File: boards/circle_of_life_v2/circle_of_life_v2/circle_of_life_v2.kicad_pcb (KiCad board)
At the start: 2 copper layers, 70.9 x 96.4 mm, 118 parts, among them IC1 ESP32-WROOM-32E-N8R2, IC2 CP2102C-A01-GQFN28, IC3 TC1262-3.3VDB, IC4 TPS565242DRLR, IC5 LT3922EUFD#PBF, J1 UART Programmer, J2 JTAG Connector, J3 Servo Motor Connector, J4 Power Connector, J5 Water Pump Connector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

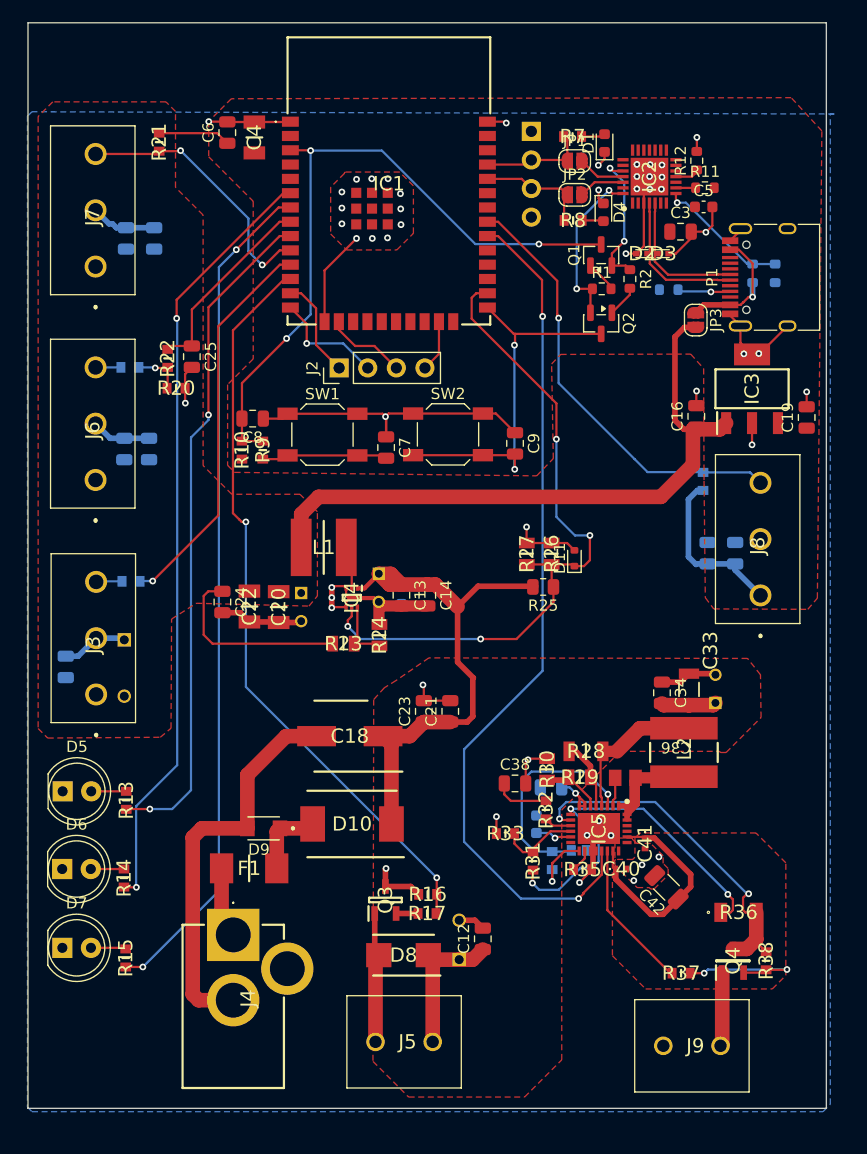
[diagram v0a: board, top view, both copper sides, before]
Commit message: Added PCB V2
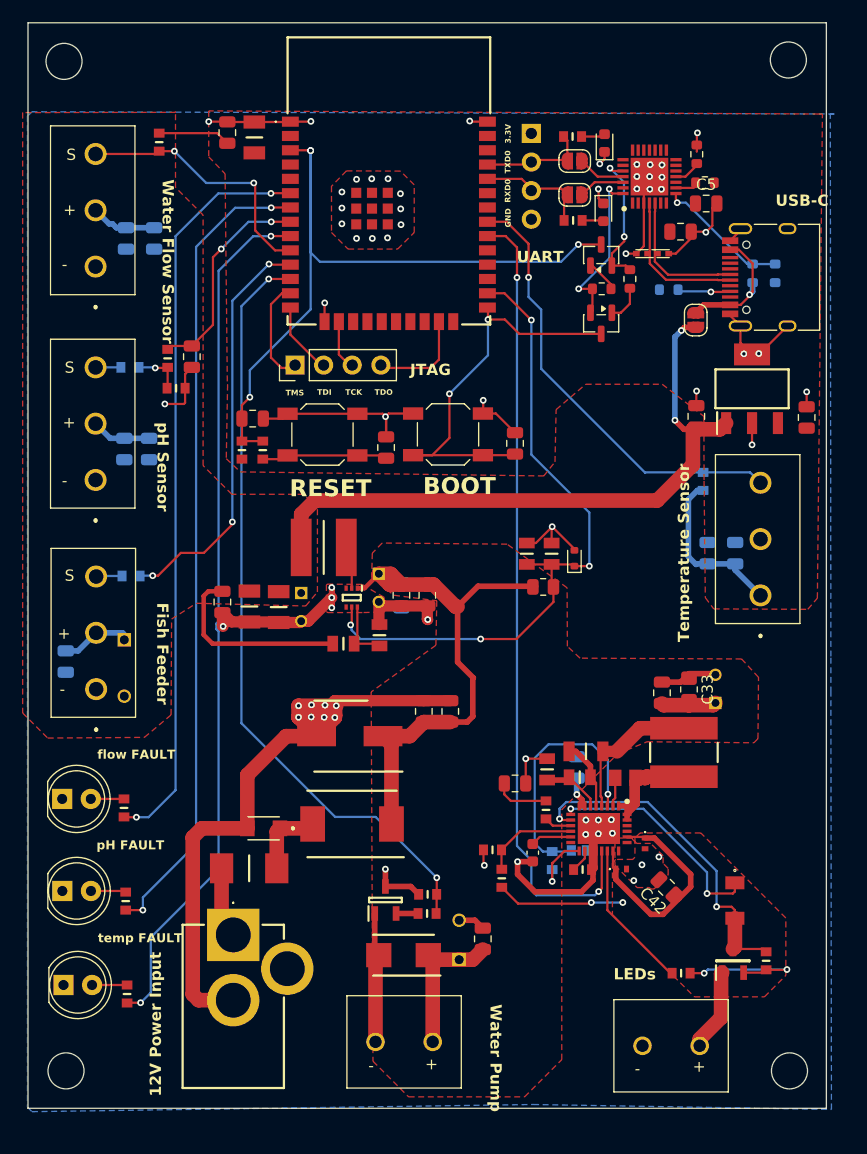
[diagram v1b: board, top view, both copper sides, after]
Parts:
- added H1: MountingHole, MountingHole:MountingHole_3.2mm_M3_ISO7380, F.Cu at (116.2, 29.3)
- added H2: MountingHole, MountingHole:MountingHole_3.2mm_M3_ISO7380, F.Cu at (180.6, 29.2)
- added H3: MountingHole, MountingHole:MountingHole_3.2mm_M3_ISO7380, F.Cu at (180.7, 119.0)
- added H4: MountingHole, MountingHole:MountingHole_3.2mm_M3_ISO7380, F.Cu at (116.4, 119.0)
- C15: footprint Capacitor_SMD:C_0603_1608Metric -> Capacitor_SMD:C_0805_2012Metric_Pad1.18x1.45mm_HandSolder
- C33: footprint SamacSys_Parts:CAPC3216X180N -> Resistor_SMD:R_0805_2012Metric_Pad1.20x1.40mm_HandSolder
- C39: moved to F.Cu
- C42: footprint Capacitor_SMD:C_1206_3216Metric -> Capacitor_SMD:C_0805_2012Metric
- C5: footprint Capacitor_SMD:C_0603_1608Metric -> Capacitor_SMD:C_0805_2012Metric
- moved R13 17.2 mm to (121.8, 112.2)
- moved D5 17.2 mm to (116.2, 111.3)
- moved D6 6.22 mm to (116.1, 94.8)
- moved R14 6.22 mm to (121.6, 95.6)
- moved D7 5.05 mm to (116.1, 103.0)
- moved R15 5.05 mm to (121.7, 103.9)
- moved J2 3.92 mm to (136.8, 56.3)
- moved R31 3.17 mm to (155.1, 101.9)
- moved C37 2.89 mm to (161.8, 92.0), turned to -90 degrees
- moved C39 2.55 mm to (157.9, 99.6), turned to 90 degrees
- moved R33 1.85 mm to (154.3, 99.3)
- moved J9 1.85 mm to (172.7, 116.8)
- moved R36 1.10 mm to (175.8, 103.8), turned to -90 degrees
- moved R12 0.57 mm to (172.4, 37.6)
- moved C1 0.47 mm to (116.4, 82.6)
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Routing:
- net GND: track 176.0 -> 204.5 mm, vias 50 -> 65
- net PH_FAULT: track 59.9 -> 76.9 mm
- net MCU_EN: track 61.5 -> 67.8 mm, vias 3 -> 4
- net PWM_DIM: track 76.6 -> 70.7 mm
- net TDO: track 4.63 -> 8.83 mm
- net TDI: track 10.1 -> 6.58 mm, vias 1 -> 0
- net INTV: track 19.9 -> 22.8 mm
- net ISP: track 54.2 -> 51.2 mm, vias 3 -> 4
- net IO0: track 33.7 -> 36.5 mm
- net TEMP_FAULT: track 75.0 -> 72.2 mm
- net TCK: track 7.23 -> 4.60 mm
- net FLOW_FAULT: track 68.9 -> 66.6 mm
- net PUMP_SGN: track 66.5 -> 68.6 mm
- net Net-(IC5-CTRL): track 4.84 -> 3.17 mm
- net SRV_SGN: track 34.8 -> 36.5 mm, vias 1 -> 3
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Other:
- board text added: "+"
- board text added: "-"
- board text added: "12V Power Input"
- board text added: "3.3V"
- board text added: "BOOT"
- board text added: "Fish Feeder"
- board text added: "GND"
- board text added: "JTAG"
- board text added: "LEDs"
- board text added: "RESET"
- board text added: "RXD0"
- board text added: "S"
- board text added: "TCK"
- board text added: "TDI"
- board text added: "TDO"
- board text added: "TMS"
- board text added: "TXD0"
- board text added: "Team 73 Circle of Life V2 Date: 3/5/26 By Aishwarya Manoj, Anjali Aravindhan, Estela Medrano"
- board text added: "Temperature Sensor"
- board text added: "UART"
- board text added: "USB-C"
- board text added: "Water Flow Sensor"
- board text added: "Water Pump"
- board text added: "flow FAULT"
- board text added: "pH FAULT"
- board text added: "pH Sensor"
- board text added: "temp FAULT"

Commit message: Routes fixed and resistors added
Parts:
- added R39: 5.1k, Resistor_SMD:R_0603_1608Metric, B.Cu at (170.0, 46.9)
- added R40: 10k, SamacSys_Parts:RESC1608X55N, B.Cu at (165.0, 100.8)
- added R41: 0, SamacSys_Parts:RESC1608X55N, B.Cu at (156.5, 50.5)
- added R42: 10k, SamacSys_Parts:RESC1608X55N, F.Cu at (163.2, 56.3)
- moved R6 2.47 mm to (181.9, 48.3)
- moved R5 2.43 mm to (179.8, 48.3)
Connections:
- IC1 pad 28: unconnected-(IC1-IO17-Pad28) -> FLOW_FAULT
- IC1 pad 29: unconnected-(IC1-IO5-Pad29) -> TEMP_FAULT
- IC1 pad 30: PWM_DIM -> Net-(IC1-IO18)
- IC1 pad 6: FLOW_FAULT -> unconnected-(IC1-IO34-Pad6)
- IC1 pad 7: TEMP_FAULT -> unconnected-(IC1-IO35-Pad7)
- P1 pad B5: unconnected-(P1-VCONN-PadB5) -> Net-(P1-CC2)
- P1 pad B6: (no net) -> D+
- P1 pad B7: (no net) -> D-
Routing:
- net TEMP_FAULT: track 72.2 -> 103.7 mm
- net FLOW_FAULT: track 66.6 -> 75.9 mm, vias 2 -> 3
- net Net-(IC1-IO18): track 0.00 -> 6.94 mm, vias 0 -> 1
- net D-: track 12.4 -> 18.3 mm
- net PWM_DIM: track 70.7 -> 64.8 mm, vias 2 -> 1
- net D+: track 13.1 -> 18.2 mm, vias 0 -> 2
- net Net-(P1-CC2): track 0.00 -> 4.65 mm, vias 0 -> 1
- net +5VBUS: track 12.1 -> 16.5 mm
- net IO0: track 36.5 -> 40.0 mm
- net VBUS: track 11.8 -> 14.3 mm
- net PUMP_SGN: track 68.6 -> 66.5 mm
- net GND: track 204.5 -> 205.4 mm, vias 65 -> 66

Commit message: Uploaded Estela notebook
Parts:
- removed JP1, JP2: Jumper_2_Open, Jumper:SolderJumper-2_P1.3mm_Open_RoundedPad1.0x1.5mm
- removed R42: 10k, SamacSys_Parts:RESC1608X55N
- added NT1: NetTie_2, NetTie:NetTie-2_SMD_Pad0.5mm, F.Cu at (161.8, 39.5)
- added NT2: NetTie_2, NetTie:NetTie-2_SMD_Pad0.5mm, F.Cu at (161.8, 40.2)
- added R43: 10k, Resistor_SMD:R_0603_1608Metric, F.Cu at (163.3, 56.2)
- moved D1 1.20 mm to (163.1, 36.6)
- moved R8 0.90 mm to (161.2, 42.6), turned to -90 degrees
- moved D4 0.85 mm to (163.3, 42.7)
- moved R7 0.78 mm to (161.1, 36.7), turned to 90 degrees
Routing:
- net GND: track 205.4 -> 204.4 mm, vias 66 -> 65
- net RX: track 4.21 -> 3.69 mm
